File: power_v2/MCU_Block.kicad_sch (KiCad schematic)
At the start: 25 parts, among them J1 USB_C_Receptacle_USB2.0, J13 Extra, Q10 S8050, Q9 S8050, U1 ESP32-WROOM, U11 CP2102-GM

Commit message: Han Board MCU va board Display
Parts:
- added SW1: button_2pin, Button_Switch_SMD:SW_DIP_SPSTx01_Slide_6.7x4.1mm_W8.61mm_P2.54mm_LowProfile, symbol Lib_Ph:button_2pin
- C31: value 100nF -> 10uF
- Q10, Q9: value S8050 -> C1815
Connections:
- net +3.3V is gone; now on net +3V3: C31.1, C31.1, U11.6 (VDD), U11.7 (REGIN)
- net ESP_IO0: now also SW1.2
- net ESP_RX: now also U1.34 (RXD0); no longer U1.35 (TXD0)
- net ESP_TX: now also U1.35 (TXD0); no longer U1.34 (RXD0)
- net GND: now also SW1.1
- no-connect marks 10 -> 11
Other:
- note added: "R = 470 OHm có thể thay R = 402 OHm"
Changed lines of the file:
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@@
   (junction (at 79.248 130.683) (diameter 0) (color 0 0 0 0)
   )
+  (junction (at 210.058 39.624) (diameter 0) (color 0 0 0 0)
+  )
   (junction (at 170.688 41.783) (diameter 0) (color 0 0 0 0)
   )
@@
   )
   (junction (at 199.517 39.624) (diameter 0) (color 0 0 0 0)
+  )
+  (junction (at 199.517 51.308) (diameter 0) (color 0 0 0 0)
   )
   (junction (at 109.728 150.495) (diameter 0) (color 0 0 0 0)
@@
   (no_connect (at 68.326 163.449))
   (no_connect (at 187.96 122.428))
+  (no_connect (at 172.466 107.696))
   (wire (pts (xy 59.436 84.582) (xy 59.436 87.376))
     (stroke (width 0) (type default))
@@
     (stroke (width 0) (type default))
   )
+  (wire (pts (xy 199.517 51.308) (xy 199.517 49.784))
+    (stroke (width 0) (type default))
+  )
   (wire (pts (xy 24.638 150.495) (xy 32.766 150.495))
     (stroke (width 0) (type default))
   )
+  (wire (pts (xy 199.517 52.959) (xy 199.517 51.308))
+    (stroke (width 0) (type default))
+  )
   (wire (pts (xy 72.136 130.683) (xy 79.248 130.683))
     (stroke (width 0) (type default))
@@
     (stroke (width 0) (type default))
   )
+  (wire (pts (xy 210.058 39.624) (xy 199.517 39.624))
+    (stroke (width 0) (type default))
+  )
   (wire (pts (xy 59.436 82.042) (xy 59.436 84.582))
     (stroke (width 0) (type default))
@@
     (stroke (width 0) (type default))
   )
-  (wire (pts (xy 204.597 39.624) (xy 199.517 39.624))
+  (wire (pts (xy 214.376 39.624) (xy 210.058 39.624))
     (stroke (width 0) (type default))
   )
@@
     (stroke (width 0) (type default))
   )
+  (wire (pts (xy 210.058 39.624) (xy 210.058 41.148))
+    (stroke (width 0) (type default))
+  )
   (wire (pts (xy 69.088 60.452) (xy 69.088 61.722))
     (stroke (width 0) (type default))
@@
     (stroke (width 0) (type default))
   )
+  (wire (pts (xy 199.517 51.308) (xy 210.058 51.308))
+    (stroke (width 0) (type default))
+  )
   (wire (pts (xy 68.326 158.115) (xy 76.2 158.115))
     (stroke (width 0) (type default))
@@
   (wire (pts (xy 69.85 168.529) (xy 69.85 170.053))
     (stroke (width 0) (type default))
+  )
+  (text "R = 470 OHm có thể thay R = 402 OHm" (at 78.486 183.642 0)
+    (effects (font (size 1.27 1.27)) (justify left bottom))
   )
   (text "ESP32-WROOM" (at 150.622 19.812 0)
@@
     )
   )
-  (global_label "ESP_IO0" (shape input) (at 204.597 39.624 0) (fields_autoplaced)
+  (global_label "ESP_IO0" (shape input) (at 214.376 39.624 0) (fields_autoplaced)
     (effects (font (size 1.27 1.27)) (justify left))
-    (property "Intersheetrefs" "${INTERSHEET_REFS}" (at 214.7511 39.5446 0)
+    (property "Intersheetrefs" "${INTERSHEET_REFS}" (at 224.5301 39.5446 0)
       (effects (font (size 1.27 1.27)) (justify left) hide)
     )
@@
     (effects (font (size 1.27 1.27)) (justify right))
   )
+  (hierarchical_label "ESP_RX" (shape input) (at 207.01 84.328 0) (fields_autoplaced)
+    (effects (font (size 1.27 1.27)) (justify left))
+  )
   (hierarchical_label "ESP_RX" (shape input) (at 106.934 177.673 0) (fields_autoplaced)
     (effects (font (size 1.27 1.27)) (justify left))
@@
     (effects (font (size 1.27 1.27)) (justify left))
   )
-  (hierarchical_label "ESP_RX" (shape input) (at 207.01 81.788 0) (fields_autoplaced)
-    (effects (font (size 1.27 1.27)) (justify left))
-  )
   (hierarchical_label "SPI_MOSI" (shape input) (at 175.26 122.428 270) (fields_autoplaced)
     (effects (font (size 1.27 1.27)) (justify right))
@@
     (effects (font (size 1.27 1.27)) (justify left))
   )
-  (hierarchical_label "ESP_TX" (shape input) (at 207.01 84.328 0) (fields_autoplaced)
-    (effects (font (size 1.27 1.27)) (justify left))
-  )
   (hierarchical_label "I2C_SDA" (shape input) (at 223.52 86.868 0) (fields_autoplaced)
     (effects (font (size 1.27 1.27)) (justify left))
   )
+  (hierarchical_label "ESP_TX" (shape input) (at 207.01 81.788 0) (fields_autoplaced)
+    (effects (font (size 1.27 1.27)) (justify left))
+  )
   (hierarchical_label "SPI_CLK" (shape input) (at 160.02 108.458 180) (fields_autoplaced)
     (effects (font (size 1.27 1.27)) (justify right))
@@
       (effects (font (size 1.27 1.27)) (justify left))
     )
-    (property "Value" "100nF" (at 102.87 157.607 0)
+    (property "Value" "10uF" (at 102.87 157.607 0)
       (effects (font (size 1.27 1.27)) (justify left))
     )
@@
     )
   )
+  (symbol (lib_id "Lib_Ph:button_2pin") (at 212.598 46.228 90) (unit 1)
+    (in_bom yes) (on_board yes) (dnp no) (fields_autoplaced)
+    (property "Reference" "SW1" (at 211.201 45.593 90)
+      (effects (font (size 1.27 1.27)) (justify right))
+    )
+    (property "Value" "button_2pin" (at 211.201 48.133 90)
+      (effects (font (size 1.27 1.27)) (justify right))
+    )
+    (property "Footprint" "Button_Switch_SMD:SW_DIP_SPSTx01_Slide_6.7x4.1mm_W8.61mm_P2.54mm_LowProfile" (at 212.598 46.228 0)
+      (effects (font (size 1.27 1.27)) hide)
+    )
+    (property "Datasheet" "" (at 212.598 46.228 0)
+      (effects (font (size 1.27 1.27)) hide)
+    )
+    (pin "1")
+    (pin "2")
+    (instances
+      (project "ph_portable_refrigerator_v2_hw"
+        (path "/e63e39d7-6ac0-4ffd-8aa3-1841a4541b55/c6ee87ef-c224-4bd4-a3c8-e8c5722a78fc"
+          (reference "SW1") (unit 1)
+        )
+      )
+    )
+  )
+  (symbol (lib_id "power:+3V3") (at 91.186 141.859 0) (unit 1)
+    (in_bom yes) (on_board yes) (dnp no)
+    (property "Reference" "#PWR01" (at 91.186 145.669 0)
+      (effects (font (size 1.27 1.27)) hide)
+    )
+    (property "Value" "+3V3" (at 91.186 138.049 0)
+      (effects (font (size 1.27 1.27)))
+    )
+    (property "Footprint" "" (at 91.186 141.859 0)
+      (effects (font (size 1.27 1.27)) hide)
+    )
+    (property "Datasheet" "" (at 91.186 141.859 0)
+      (effects (font (size 1.27 1.27)) hide)
+    )
+    (pin "1")
+    (instances
+      (project "ph_portable_refrigerator_v2_hw"
+        (path "/e63e39d7-6ac0-4ffd-8aa3-1841a4541b55"
+          (reference "#PWR01") (unit 1)
+        )
+        (path "/e63e39d7-6ac0-4ffd-8aa3-1841a4541b55/c6ee87ef-c224-4bd4-a3c8-e8c5722a78fc"
+          (reference "#PWR0120") (unit 1)
+        )
+      )
+    )
+  )
   (symbol (lib_id "1ph_lib:R0603") (at 170.688 37.973 180) (unit 1)
     (in_bom yes) (on_board yes) (dnp no)
@@
         (path "/e63e39d7-6ac0-4ffd-8aa3-1841a4541b55/c6ee87ef-c224-4bd4-a3c8-e8c5722a78fc"
           (reference "#PWR0105") (unit 1)
-        )
-      )
-    )
-  )
-  (symbol (lib_id "power:+3.3V") (at 91.186 141.859 0) (unit 1)
-    (in_bom yes) (on_board yes) (dnp no)
-    (property "Reference" "#PWR0105" (at 91.186 145.669 0)
-      (effects (font (size 1.27 1.27)) hide)
-    )
-    (property "Value" "+3.3V" (at 90.17 138.049 0)
-      (effects (font (size 1.27 1.27)))
-    )
-    (property "Footprint" "" (at 91.186 141.859 0)
-      (effects (font (size 1.27 1.27)) hide)
-    )
-    (property "Datasheet" "" (at 91.186 141.859 0)
-      (effects (font (size 1.27 1.27)) hide)
-    )
-    (pin "1")
-    (instances
-      (project "Esp32_Presence_Sensor_hw"
-        (path "/512eb577-9d66-4922-b649-256857904c1b"
-          (reference "#PWR0105") (unit 1)
-        )
-      )
-      (project "Esp32_Modbus_Relay_hw_V2"
-        (path "/b38a1678-1962-46d5-83ec-ed2581563ddd"
-          (reference "#PWR075") (unit 1)
-        )
-      )
-      (project "ph_portable_refrigerator_v2_hw"
-        (path "/e63e39d7-6ac0-4ffd-8aa3-1841a4541b55/c6ee87ef-c224-4bd4-a3c8-e8c5722a78fc"
-          (reference "#PWR0138") (unit 1)
         )
       )
@@
       (effects (font (size 1.27 1.27)) (justify left))
     )
-    (property "Value" "S8050" (at 102.362 128.778 0)
+    (property "Value" "C1815" (at 102.362 128.778 0)
       (effects (font (size 1.27 1.27)) (justify left))
     )
@@
       (effects (font (size 1.27 1.27)) (justify left))
     )
-    (property "Value" "100nF" (at 84.328 157.099 0)
+    (property "Value" "10uF" (at 84.328 157.099 0)
       (effects (font (size 1.27 1.27)) (justify left))
     )
@@
   (symbol (lib_id "Device:Q_NPN_BEC") (at 96.52 115.189 0) (unit 1)
     (in_bom yes) (on_board yes) (dnp no) (fields_autoplaced)
-    (property "Reference" "Q9" (at 102.362 114.554 0)
-      (effects (font (size 1.27 1.27)) (justify left))
-    )
-    (property "Value" "S8050" (at 102.362 117.094 0)
+    (property "Reference" "Q9" (at 101.6 114.554 0)
+      (effects (font (size 1.27 1.27)) (justify left))
+    )
+    (property "Value" "C1815" (at 101.6 117.094 0)
       (effects (font (size 1.27 1.27)) (justify left))
     )
@@
     )
   )
-  (symbol (lib_id "power:GND") (at 199.517 49.784 0) (unit 1)
-    (in_bom yes) (on_board yes) (dnp no)
-    (property "Reference" "#PWR023" (at 199.517 56.134 0)
-      (effects (font (size 1.27 1.27)) hide)
-    )
-    (property "Value" "GND" (at 199.517 56.769 90)
-      (effects (font (size 1.27 1.27)) (justify left))
-    )
-    (property "Footprint" "" (at 199.517 49.784 0)
-      (effects (font (size 1.27 1.27)) hide)
-    )
-    (property "Datasheet" "" (at 199.517 49.784 0)
-      (effects (font (size 1.27 1.27)) hide)
-    )
+  (symbol (lib_id "power:GND") (at 199.517 52.959 0) (unit 1)
+    (in_bom yes) (on_board yes) (dnp no)
+    (property "Reference" "#PWR023" (at 199.517 59.309 0)
+      (effects (font (size 1.27 1.27)) hide)
+    )
+    (property "Value" "GND" (at 199.517 59.944 90)
+      (effects (font (size 1.27 1.27)) (justify left))
+    )
+    (property "Footprint" "" (at 199.517 52.959 0)
+      (effects (font (size 1.27 1.27)) hide)
+    )
+    (property "Datasheet" "" (at 199.517 52.959 0)
+      (effects (font (size 1.27 1.27)) hide)
+    )

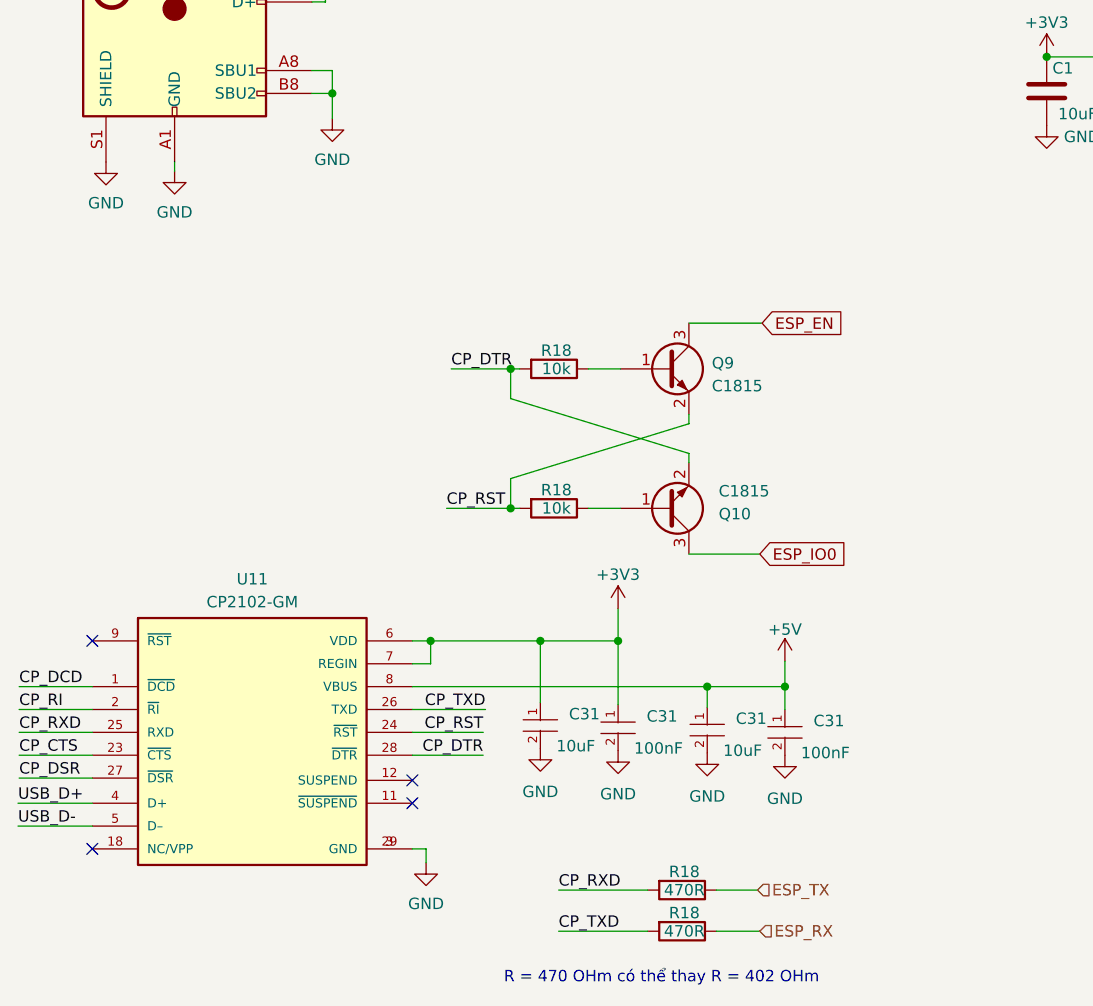
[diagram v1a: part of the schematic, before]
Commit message: Modify tx/rx UART0, LED GPS, pin rst/clk sim card
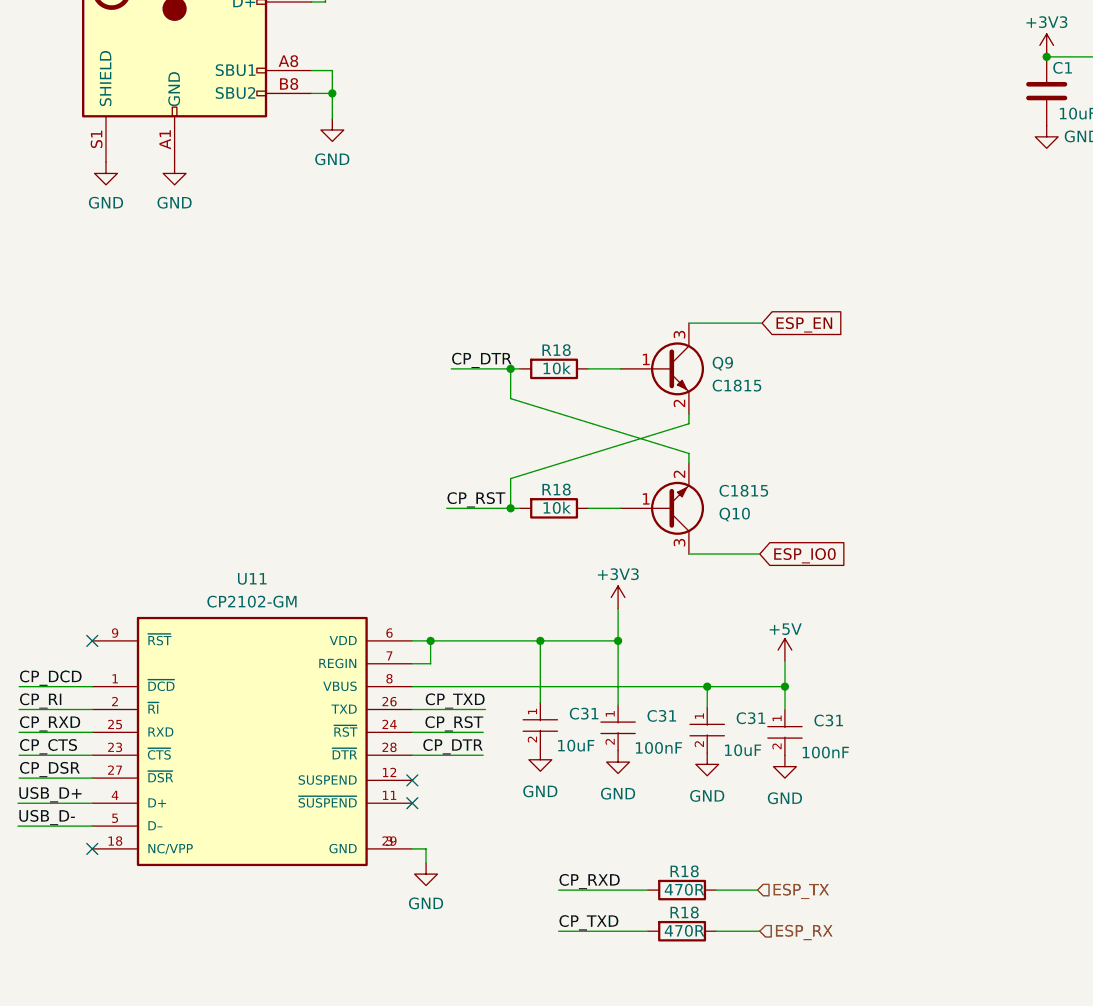
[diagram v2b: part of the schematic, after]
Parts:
- SW1: footprint Button_Switch_SMD:SW_DIP_SPSTx01_Slide_6.7x4.1mm_W8.61mm_P2.54mm_LowProfile -> Button_Switch_SMD:SW_DIP_SPSTx01_Slide_6.7x4.1mm_W6.73mm_P2.54mm_LowProfile_JPin
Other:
- note removed: "R = 470 OHm có thể thay R = 402 OHm"
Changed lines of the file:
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@@
-    (stroke (width 0) (type default))
-  )
-  (wire (pts (xy 41.91 92.202) (xy 41.91 93.218))
     (stroke (width 0) (type default))
   )
@@
   (wire (pts (xy 69.85 168.529) (xy 69.85 170.053))
     (stroke (width 0) (type default))
-  )
-  (text "R = 470 OHm có thể thay R = 402 OHm" (at 78.486 183.642 0)
-    (effects (font (size 1.27 1.27)) (justify left bottom))
   )
   (text "ESP32-WROOM" (at 150.622 19.812 0)
@@
       (effects (font (size 1.27 1.27)) (justify right))
     )
-    (property "Footprint" "Button_Switch_SMD:SW_DIP_SPSTx01_Slide_6.7x4.1mm_W8.61mm_P2.54mm_LowProfile" (at 212.598 46.228 0)
+    (property "Footprint" "Button_Switch_SMD:SW_DIP_SPSTx01_Slide_6.7x4.1mm_W6.73mm_P2.54mm_LowProfile_JPin" (at 212.598 46.228 0)
       (effects (font (size 1.27 1.27)) hide)
     )
@@
     )
   )
-  (symbol (lib_name "GND_2") (lib_id "power:GND") (at 41.91 93.218 0) (unit 1)
-    (in_bom yes) (on_board yes) (dnp no) (fields_autoplaced)
-    (property "Reference" "#PWR091" (at 41.91 99.568 0)
-      (effects (font (size 1.27 1.27)) hide)
-    )
-    (property "Value" "GND" (at 41.91 97.79 0)
-      (effects (font (size 1.27 1.27)))
-    )
-    (property "Footprint" "" (at 41.91 93.218 0)
-      (effects (font (size 1.27 1.27)) hide)
-    )
-    (property "Datasheet" "" (at 41.91 93.218 0)
-      (effects (font (size 1.27 1.27)) hide)
-    )
+  (symbol (lib_name "GND_2") (lib_id "power:GND") (at 41.91 92.202 0) (unit 1)
+    (in_bom yes) (on_board yes) (dnp no) (fields_autoplaced)
+    (property "Reference" "#PWR091" (at 41.91 98.552 0)
+      (effects (font (size 1.27 1.27)) hide)
+    )
+    (property "Value" "GND" (at 41.91 96.774 0)
+      (effects (font (size 1.27 1.27)))
+    )
+    (property "Footprint" "" (at 41.91 92.202 0)
+      (effects (font (size 1.27 1.27)) hide)
+    )
+    (property "Datasheet" "" (at 41.91 92.202 0)
+      (effects (font (size 1.27 1.27)) hide)
+    )
